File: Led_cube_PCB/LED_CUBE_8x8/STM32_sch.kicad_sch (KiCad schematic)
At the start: 17 parts, among them IC29 STM32C071C8T6, IC30 TPS562202DRLR

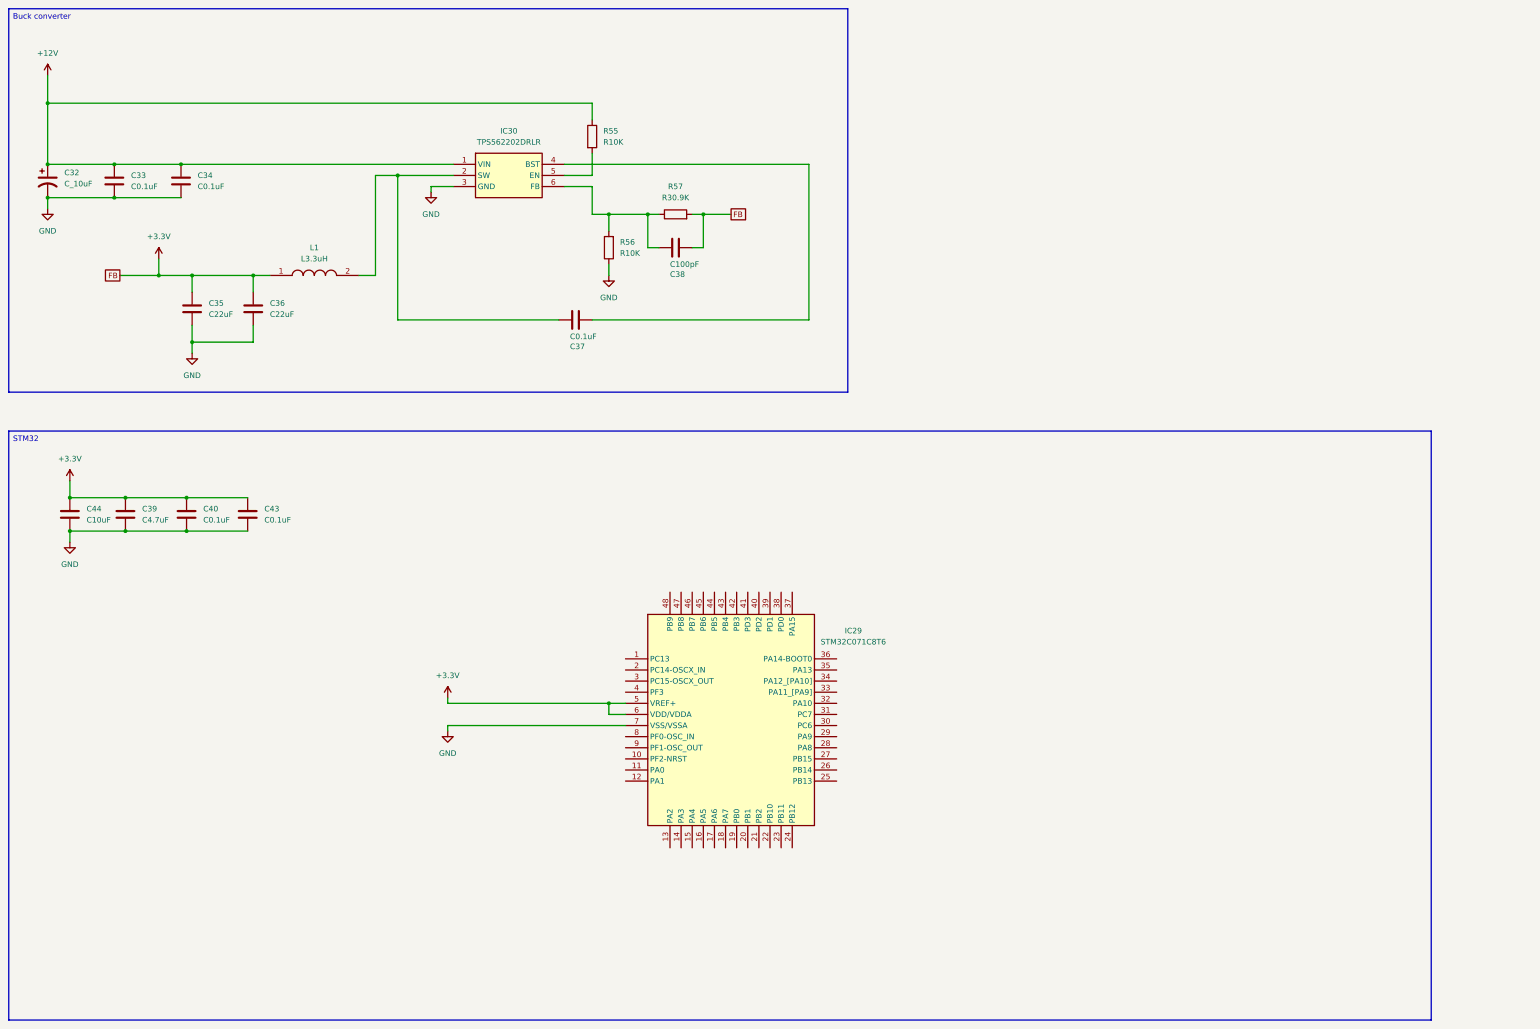
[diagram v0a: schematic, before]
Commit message: WIP: need to add connectors for the LED channels
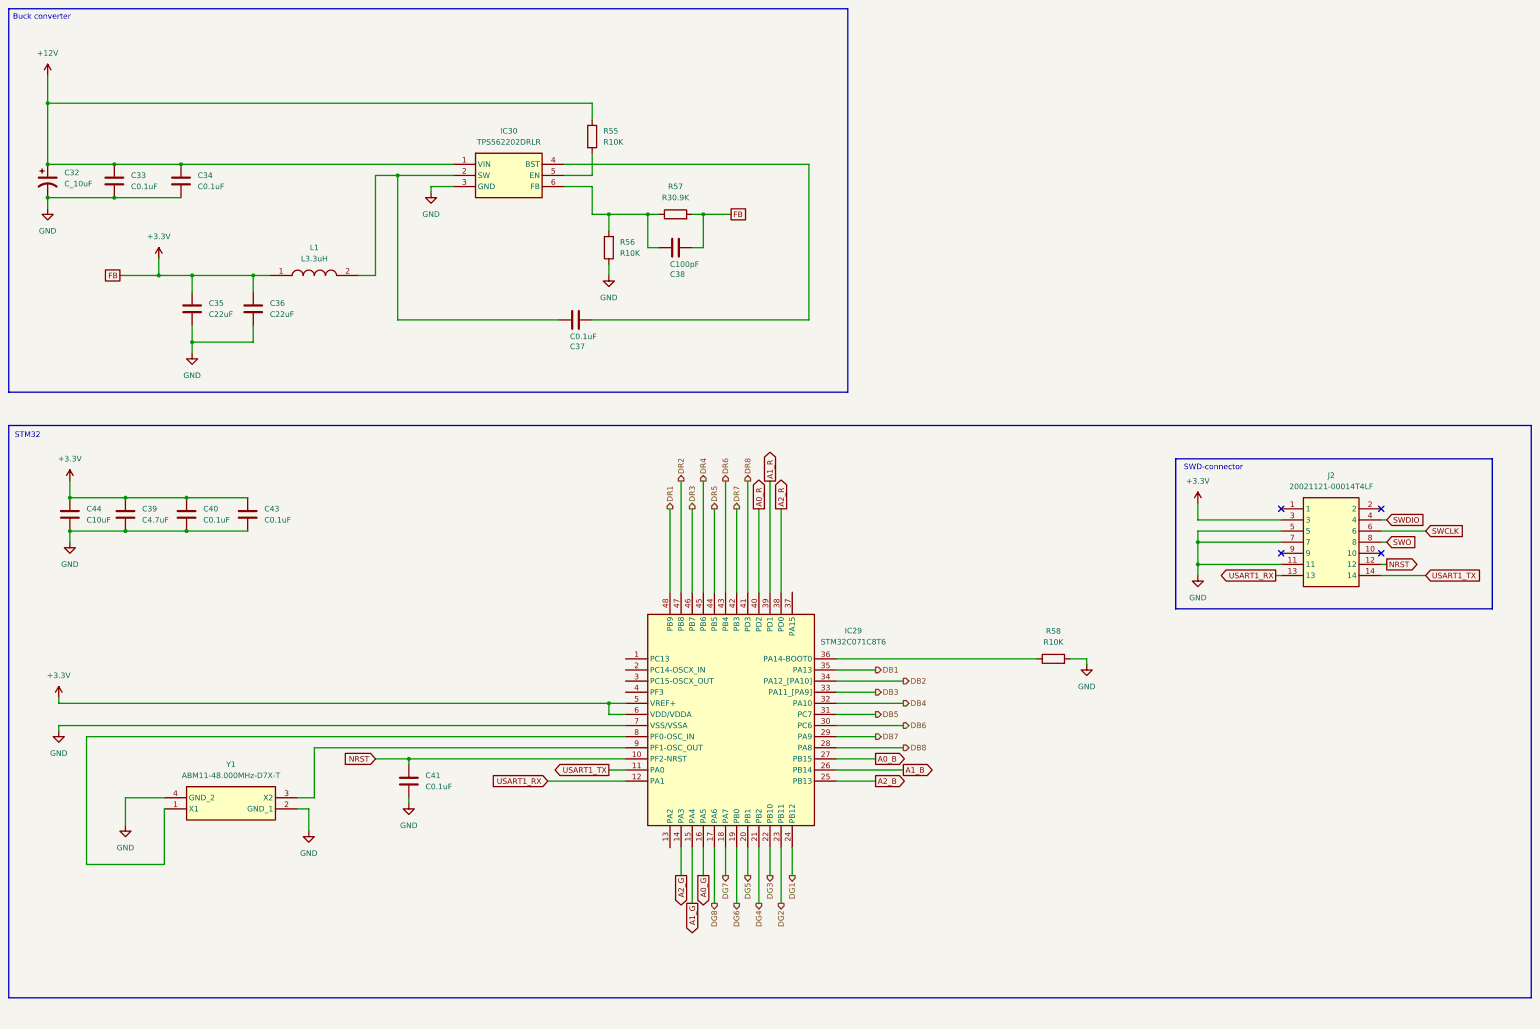
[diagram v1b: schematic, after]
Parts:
- added C41: C0.1uF, symbol Device:C
- added J2: 20021121-00014T4LF, 2002112100014T4LF, symbol SamacSys_Parts:20021121-00014T4LF
- added R58: R10K, symbol Device:R
- added Y1: ABM11-48.000MHz-D7X-T, ABM11, symbol SamacSys_Parts:ABM11-48.000MHz-D7X-T
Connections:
- net +3.3V: now also J2.3
- net GND: now also C41.2, J2.11, J2.5, J2.7, R58.2, Y1.2 (GND_1), Y1.4 (GND_2)
- net NRST: now reaches IC29.10 (PF2-NRST)
- net NRST: now also C41.1, J2.12
- net USART1_TX: now reaches IC29.11 (PA0)
- net USART1_TX: now also J2.14
- net USART1_RX: now reaches IC29.12 (PA1)
- net USART1_RX: now also J2.13
- net A2_G: now reaches IC29.14 (PA3)
- net A1_G: now reaches IC29.15 (PA4)
- net A0_G: now reaches IC29.16 (PA5)
- net DG8: now reaches IC29.17 (PA6)
- net DG7: now reaches IC29.18 (PA7)
- net DG6: now reaches IC29.19 (PB0)
- net DG5: now reaches IC29.20 (PB1)
- net DG4: now reaches IC29.21 (PB2)
- net DG3: now reaches IC29.22 (PB10)
- net DG2: now reaches IC29.23 (PB11)
- net DG1: now reaches IC29.24 (PB12)
- net A2_B: now reaches IC29.25 (PB13)
- net A1_B: now reaches IC29.26 (PB14)
- net A0_B: now reaches IC29.27 (PB15)
- net DB8: now reaches IC29.28 (PA8)
- net DB7: now reaches IC29.29 (PA9)
- net DB6: now reaches IC29.30 (PC6)
- net DB5: now reaches IC29.31 (PC7)
- net DB4: now reaches IC29.32 (PA10)
- net DB3: now reaches IC29.33 (PA11_[PA9])
- net DB2: now reaches IC29.34 (PA12_[PA10])
- net DB1: now reaches IC29.35 (PA13)
- net at IC29.36 (PA14-BOOT0): now also R58.1
- net A2_R: now reaches IC29.38 (PD0)
- net A1_R: now reaches IC29.39 (PD1)
- net A0_R: now reaches IC29.40 (PD2)
- net DR8: now reaches IC29.41 (PD3)
- net DR7: now reaches IC29.42 (PB3)
- net DR6: now reaches IC29.43 (PB4)
- net DR5: now reaches IC29.44 (PB5)
- net DR4: now reaches IC29.45 (PB6)
- net DR3: now reaches IC29.46 (PB7)
- net DR2: now reaches IC29.47 (PB8)
- net DR1: now reaches IC29.48 (PB9)
- net at IC29.8 (PF0-OSC_IN): now also Y1.1 (X1)
- net at IC29.9 (PF1-OSC_OUT): now also Y1.3 (X2)
- new net SWCLK: J2.6
- new net SWDIO: J2.4
- new net SWO: J2.8
- no-connect marks 0 -> 4
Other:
- note added: "STM32"
- note added: "SWD-connector"

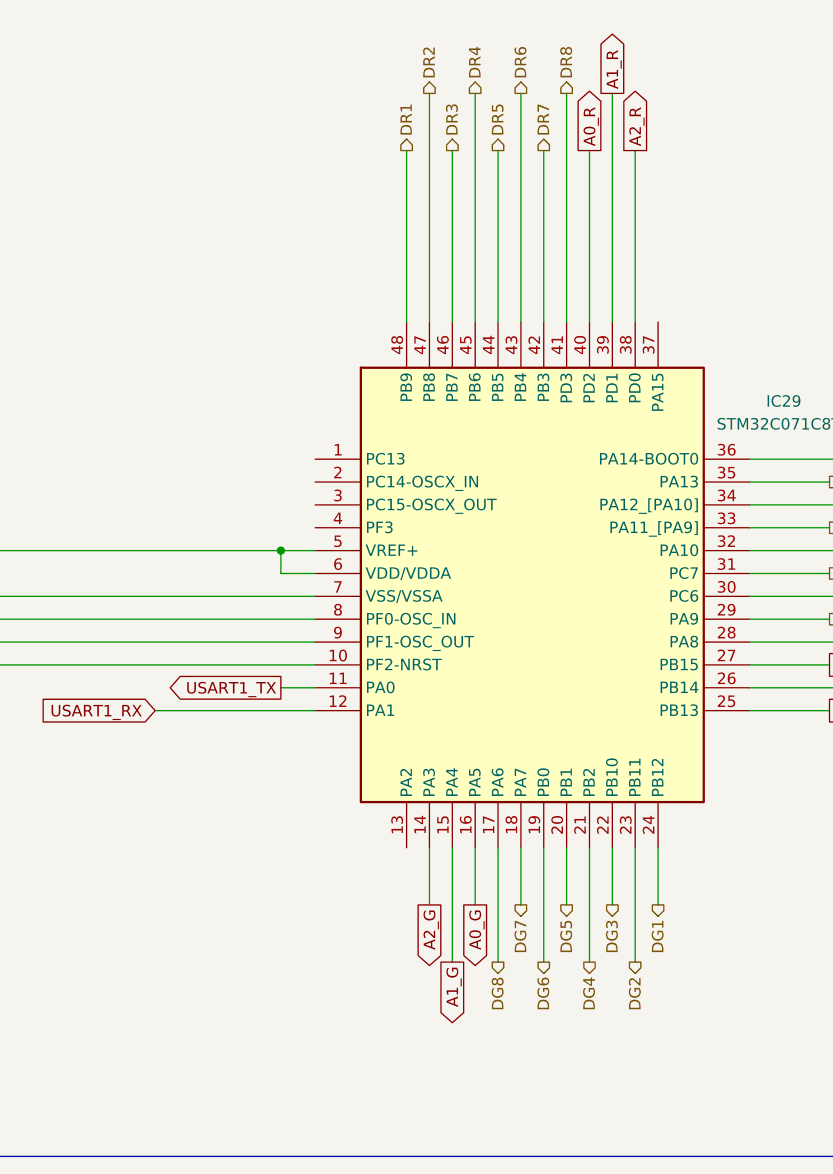
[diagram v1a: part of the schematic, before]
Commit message: WIP: added layer select schematic
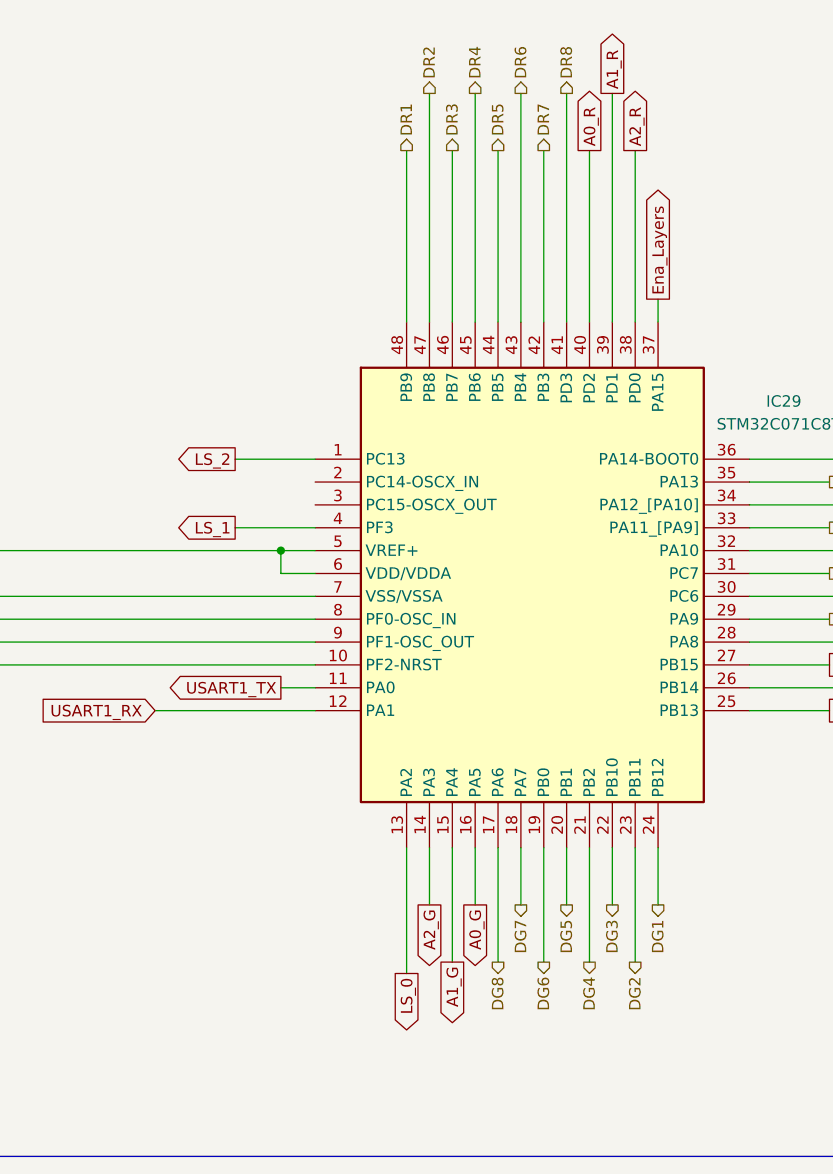
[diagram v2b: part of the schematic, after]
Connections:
- net LS_2: now reaches IC29.1 (PC13)
- net LS_0: now reaches IC29.13 (PA2)
- net Ena_Layers: now reaches IC29.37 (PA15)
- net LS_1: now reaches IC29.4 (PF3)
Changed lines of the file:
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@@
+	(wire
+		(pts
+			(xy 147.32 162.56) (xy 156.21 162.56)
+		)
+		(stroke
+			(width 0)
+			(type default)
+		)
+	)
 	(wire
 		(pts
@@
 	(wire
 		(pts
+			(xy 147.32 170.18) (xy 156.21 170.18)
+		)
+		(stroke
+			(width 0)
+			(type default)
+		)
+	)
+	(wire
+		(pts
 			(xy 304.8 143.51) (xy 306.07 143.51)
 		)
@@
 	(wire
 		(pts
+			(xy 166.37 205.74) (xy 166.37 219.71)
+		)
+		(stroke
+			(width 0)
+			(type default)
+		)
+	)
+	(wire
+		(pts
 			(xy 181.61 128.27) (xy 181.61 147.32)
 		)
@@
 		(pts
 			(xy 306.07 133.35) (xy 287.02 133.35)
+		)
+		(stroke
+			(width 0)
+			(type default)
+		)
+	)
+	(wire
+		(pts
+			(xy 194.31 144.78) (xy 194.31 147.32)
 		)
 		(stroke
@@
 		)
 	)
+	(global_label "LS_2"
+		(shape output)
+		(at 147.32 162.56 180)
+		(fields_autoplaced yes)
+		(effects
+			(font
+				(size 1.27 1.27)
+			)
+			(justify right)
+		)
+		(property "Intersheetrefs" "${INTERSHEET_REFS}"
+			(at 139.9201 162.56 0)
+			(effects
+				(font
+					(size 1.27 1.27)
+				)
+				(justify right)
+				(hide yes)
+			)
+		)
+	)
 	(global_label "USART1_RX"
 		(shape output)
@@
 		)
 	)
+	(global_label "Ena_Layers"
+		(shape output)
+		(at 194.31 144.78 90)
+		(fields_autoplaced yes)
+		(effects
+			(font
+				(size 1.27 1.27)
+			)
+			(justify left)
+		)
+		(property "Intersheetrefs" "${INTERSHEET_REFS}"
+			(at 194.31 131.3326 90)
+			(effects
+				(font
+					(size 1.27 1.27)
+				)
+				(justify left)
+				(hide yes)
+			)
+		)
+	)
 	(global_label "USART1_TX"
 		(shape input)
@@
 		)
 	)
+	(global_label "LS_0"
+		(shape output)
+		(at 166.37 219.71 270)
+		(fields_autoplaced yes)
+		(effects
+			(font
+				(size 1.27 1.27)
+			)
+			(justify right)
+		)
+		(property "Intersheetrefs" "${INTERSHEET_REFS}"
+			(at 166.37 227.1099 90)
+			(effects
+				(font
+					(size 1.27 1.27)
+				)
+				(justify right)
+				(hide yes)
+			)
+		)
+	)
 	(global_label "A1_B"
 		(shape output)
@@
 			(effects
 				(font
+					(size 1.27 1.27)
+				)
+				(justify right)
+				(hide yes)
+			)
+		)
+	)
+	(global_label "LS_1"
+		(shape output)
+		(at 147.32 170.18 180)
+		(fields_autoplaced yes)
+		(effects
+			(font
+				(size 1.27 1.27)
+			)
+			(justify right)
+		)
+		(property "Intersheetrefs" "${INTERSHEET_REFS}"
+			(at 139.9201 170.18 0)
+			(effects
+				(font
